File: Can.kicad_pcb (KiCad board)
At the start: 2 copper layers, 60.2 x 48.8 mm, 52 parts, among them IC1 ATMEGA328P-A, K1 HK4100F, K2 HK4100F, P3 CONN_01X03, P4 CONN_01X03, P5 CONN_01X02, P6 CONN_01X02, Q1 BC808-40, Q2 BC808-40, SW1 SW_PUSH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

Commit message: plano de masa y vcc
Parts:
- moved P5 0.29 mm to (125.6, 80.0)
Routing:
- net +5V: track 361.3 -> 362.5 mm
- net /TX: track 66.0 -> 64.8 mm
- net /RX: track 74.9 -> 73.8 mm
- added copper zone on B.Cu, net +5V
- added copper zone on F.Cu, net GND
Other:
- net class Default: via_dia 0.6 -> 1.8; via_drill 0.4 -> 0.8

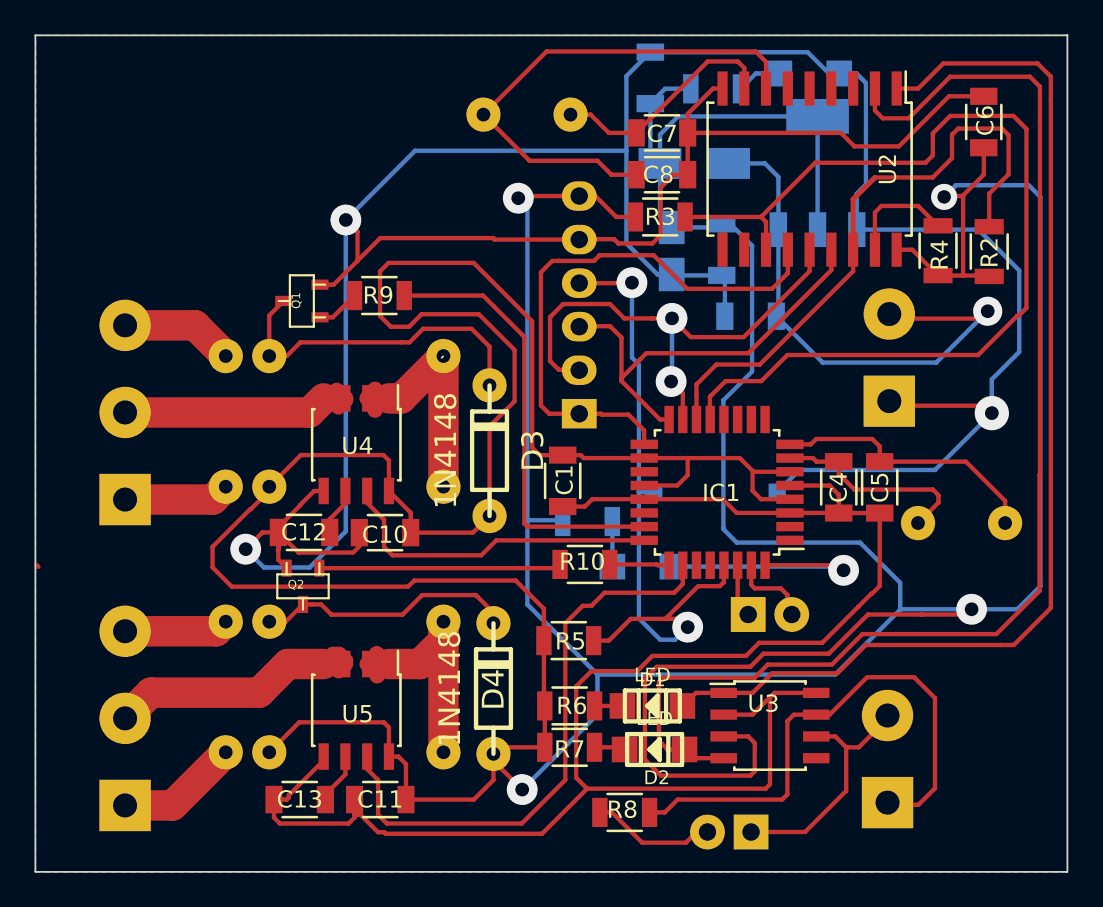
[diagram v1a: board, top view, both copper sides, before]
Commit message: fix islas 220v
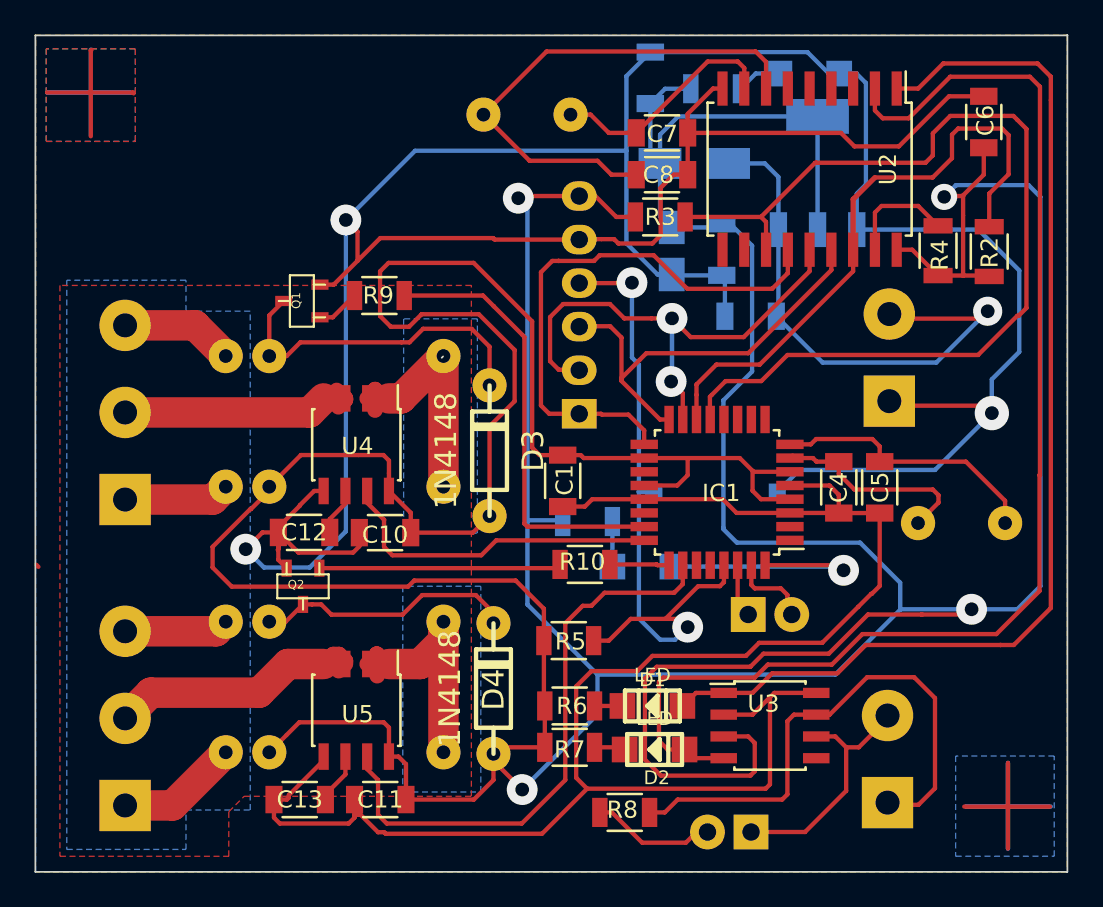
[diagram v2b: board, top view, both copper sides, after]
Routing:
- net (no net): track 0.16 -> 40.4 mm
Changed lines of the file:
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@@
     (links 125)
     (no_connects 0)
-    (area 75.718199 61.151299 136.016201 110.057401)
+    (area 75.504699 60.9034 145.940861 116.50548)
     (thickness 1.6)
     (drawings 10)
-    (tracks 635)
+    (tracks 646)
     (zones 0)
     (modules 52)
@@
   (layers
     (0 F.Cu signal)
-    (31 B.Cu signal)
+    (31 B.Cu signal hide)
     (32 B.Adhes user hide)
     (33 F.Adhes user hide)
     (34 B.Paste user hide)
     (35 F.Paste user hide)
-    (36 B.SilkS user)
+    (36 B.SilkS user hide)
     (37 F.SilkS user hide)
     (38 B.Mask user hide)
     (39 F.Mask user hide)
-    (40 Dwgs.User user)
+    (40 Dwgs.User user hide)
     (41 Cmts.User user hide)
     (42 Eco1.User user hide)
     (43 Eco2.User user hide)
     (44 Edge.Cuts user)
-    (45 Margin user)
+    (45 Margin user hide)
     (46 B.CrtYd user hide)
     (47 F.CrtYd user hide)
     (48 B.Fab user hide)
-    (49 F.Fab user)
+    (49 F.Fab user hide)
   )
   (setup
@@
     (visible_elements 7FFDD609)
     (pcbplotparams
-      (layerselection 0x3ffff_80000001)
+      (layerselection 0x00000_80000001)
       (usegerberextensions false)
       (excludeedgelayer true)
       (linewidth 0.100000)
-      (plotframeref false)
+      (plotframeref true)
       (viasonmask false)
       (mode 1)
@@
       (hpglpendiameter 15)
       (hpglpenoverlay 2)
-      (psnegative false)
+      (psnegative true)
       (psa4output false)
       (plotreference true)
-      (plotvalue true)
+      (plotvalue false)
       (plotinvisibletext false)
       (padsonsilk false)
@@
       (drillshape 0)
       (scaleselection 1)
-      (outputdirectory ""))
+      (outputdirectory CAN_doblefaz))
   )
   (net 0 "")
@@
   (gr_line (start 135.9662 110.0074) (end 75.7682 110.0074) (angle 90) (layer Edge.Cuts) (width 0.1))
   (gr_line (start 99.55276 79.93888) (end 99.4664 80.02524) (angle 90) (layer Edge.Cuts) (width 0.1))
+  (segment (start 76.45 64.55) (end 81.45 64.55) (width 0.254) (layer F.Cu) (net 0))
+  (segment (start 81.45 64.55) (end 81.5 64.6) (width 0.254) (layer F.Cu) (net 0))
+  (segment (start 79 67.1) (end 79 62.1) (width 0.254) (layer F.Cu) (net 0))
+  (segment (start 79 62.1) (end 79.05 62.05) (width 0.254) (layer F.Cu) (net 0))
+  (segment (start 129.95 106.2) (end 134.95 106.2) (width 0.254) (layer F.Cu) (net 0))
+  (segment (start 132.5 103.65) (end 132.5 108.65) (width 0.254) (layer F.Cu) (net 0))
+  (segment (start 76.45 64.55) (end 81.5 64.55) (width 0.254) (layer B.Cu) (net 0))
+  (segment (start 79 62.05) (end 79 67.05) (width 0.254) (layer B.Cu) (net 0))
+  (segment (start 130 106.2) (end 135 106.2) (width 0.254) (layer B.Cu) (net 0))
+  (segment (start 132.5 103.65) (end 132.5 108.65) (width 0.254) (layer B.Cu) (net 0))
+  (segment (start 132.5 108.65) (end 132.5 108.6) (width 0.254) (layer B.Cu) (net 0))
   (segment (start 75.8317 92.1004) (end 75.946 92.2147) (width 0.254) (layer F.Cu) (net 0))
   (segment (start 115.1128 83.6022) (end 115.1128 82.296) (width 0.254) (layer F.Cu) (net 1))
@@
     (polygon
       (pts
-        (xy 75.7809 61.214) (xy 135.9662 61.214) (xy 135.9662 110.0074) (xy 75.7682 110.0074)
+        (xy 135.9662 110.0074) (xy 75.7682 110.0074) (xy 75.7809 61.214) (xy 135.9662 61.214) (xy 135.9662 110.0074)
+      )
+    )
+    (polygon
+      (pts        (xy 77.2 75.8) (xy 77.2 109.1) (xy 87.05 109.1) (xy 87.05 106.5) (xy 87.95 105.6)
+        (xy 101.2 105.6) (xy 101.2 75.8) (xy 77.2 75.8)
+      )
+    )
+    (polygon
+      (pts        (xy 76.4 62) (xy 76.4 67.4) (xy 81.6 67.4) (xy 81.6 62) (xy 76.4 62)
       )
     )
@@
       )
     )
+    (polygon
+      (pts        (xy 129.45 103.25) (xy 129.45 109.1) (xy 135.2 109.1) (xy 135.2 103.25) (xy 129.45 103.25)
+      )
+    )
+    (polygon
+      (pts        (xy 77.6 75.5) (xy 77.6 108.7) (xy 84.55 108.7) (xy 84.55 106.4) (xy 88.3 106.4)
+        (xy 88.3 77.3) (xy 84.55 77.3) (xy 84.55 75.5) (xy 77.6 75.5)
+      )
+    )
+    (polygon
+      (pts        (xy 97.2 93.35) (xy 97.2 105.35) (xy 101.75 105.35) (xy 101.75 93.35) (xy 97.2 93.35)
+      )
+    )
+    (polygon
+      (pts        (xy 97.25 77.75) (xy 97.25 90.25) (xy 101.55 90.25) (xy 101.55 77.75) (xy 97.25 77.75)
+      )
+    )
+    (polygon
+      (pts        (xy 76.4 62) (xy 76.4 67.4) (xy 81.6 67.4) (xy 81.6 62) (xy 76.4 62)
+      )
+    )
